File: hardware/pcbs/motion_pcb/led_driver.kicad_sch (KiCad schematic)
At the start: 5 parts, among them Q1 BSS138, U42 SN74LVC1T45DBV

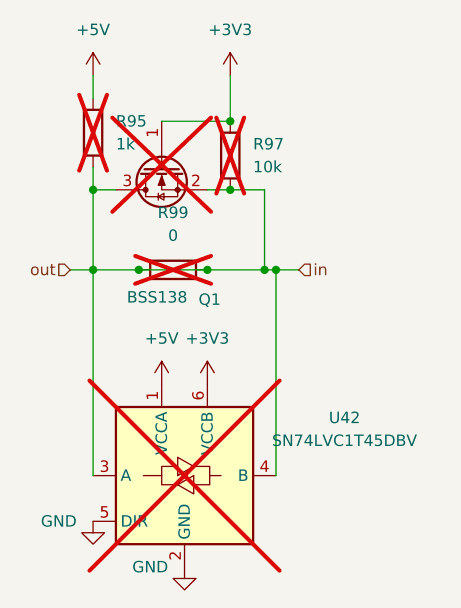
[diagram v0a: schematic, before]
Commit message: finished pcb motion.
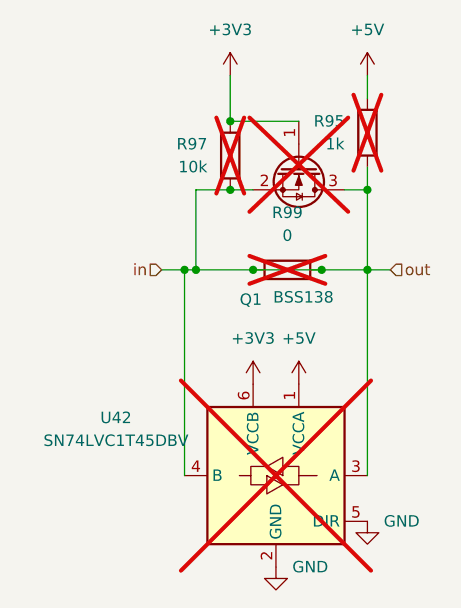
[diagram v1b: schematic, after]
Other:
- moved on the sheet: Q1, R95, R99, U42
